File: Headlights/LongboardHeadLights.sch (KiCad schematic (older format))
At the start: 16 parts, among them P1 CONN_01X03, U1 AL8805

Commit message: small schematic changes
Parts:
- C1: footprint (none) -> Capacitors_SMD:C_0805_HandSoldering
- C2: footprint (none) -> Capacitors_SMD:C_0603_HandSoldering
- D4: footprint (none) -> Light_Parts:PowerDI-123
- JP1: footprint (none) -> Connect:GS3
- L1: footprint (none) -> Light_Parts:Inductor_Bourns_6045
- P1: footprint (none) -> Connectors_Molex:Molex_KK-6410-03_03x2.54mm_Straight
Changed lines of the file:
@@
 F 0 "C2" H 3025 3200 50  0000 L CNN
 F 1 "2.2uF" H 3025 3000 50  0000 L CNN
-F 2 "" H 3038 2950 50  0001 C CNN
+F 2 "Capacitors_SMD:C_0603_HandSoldering" H 3038 2950 50  0001 C CNN
 F 3 "" H 3000 3100 50  0000 C CNN
 	1    3000 3100
@@
 F 0 "C1" H 2725 3200 50  0000 L CNN
 F 1 "4.7uF" H 2725 3000 50  0000 L CNN
-F 2 "" H 2738 2950 50  0001 C CNN
+F 2 "Capacitors_SMD:C_0805_HandSoldering" H 2738 2950 50  0001 C CNN
 F 3 "" H 2700 3100 50  0000 C CNN
 	1    2700 3100
@@
 F 0 "L1" V 4400 5100 50  0000 C CNN
 F 1 "INDUCTOR" V 4550 5100 50  0000 C CNN
-F 2 "" H 4450 5100 50  0001 C CNN
+F 2 "Light_Parts:Inductor_Bourns_6045" H 4450 5100 50  0001 C CNN
 F 3 "" H 4450 5100 50  0000 C CNN
 	1    4450 5100
@@
 F 0 "D4" H 5050 3750 50  0000 C CNN
 F 1 "D_Schottky" H 5050 3550 50  0000 C CNN
-F 2 "" H 5050 3650 50  0001 C CNN
+F 2 "Light_Parts:PowerDI-123" H 5050 3650 50  0001 C CNN
 F 3 "" H 5050 3650 50  0000 C CNN
 	1    5050 3650
@@
 F 0 "JP1" H 6300 2850 50  0000 L CNN
 F 1 "JUMPER3" H 6250 3050 50  0000 C BNN
-F 2 "" H 6250 2950 50  0001 C CNN
+F 2 "Connect:GS3" H 6250 2950 50  0001 C CNN
 F 3 "" H 6250 2950 50  0000 C CNN
 	1    6250 2950
@@
 F 0 "P1" H 7800 2800 50  0000 C CNN
 F 1 "CONN_01X03" V 7900 2600 50  0000 C CNN
-F 2 "" H 7800 2600 50  0001 C CNN
+F 2 "Connectors_Molex:Molex_KK-6410-03_03x2.54mm_Straight" H 7800 2600 50  0001 C CNN
 F 3 "" H 7800 2600 50  0000 C CNN
 	1    7800 2600

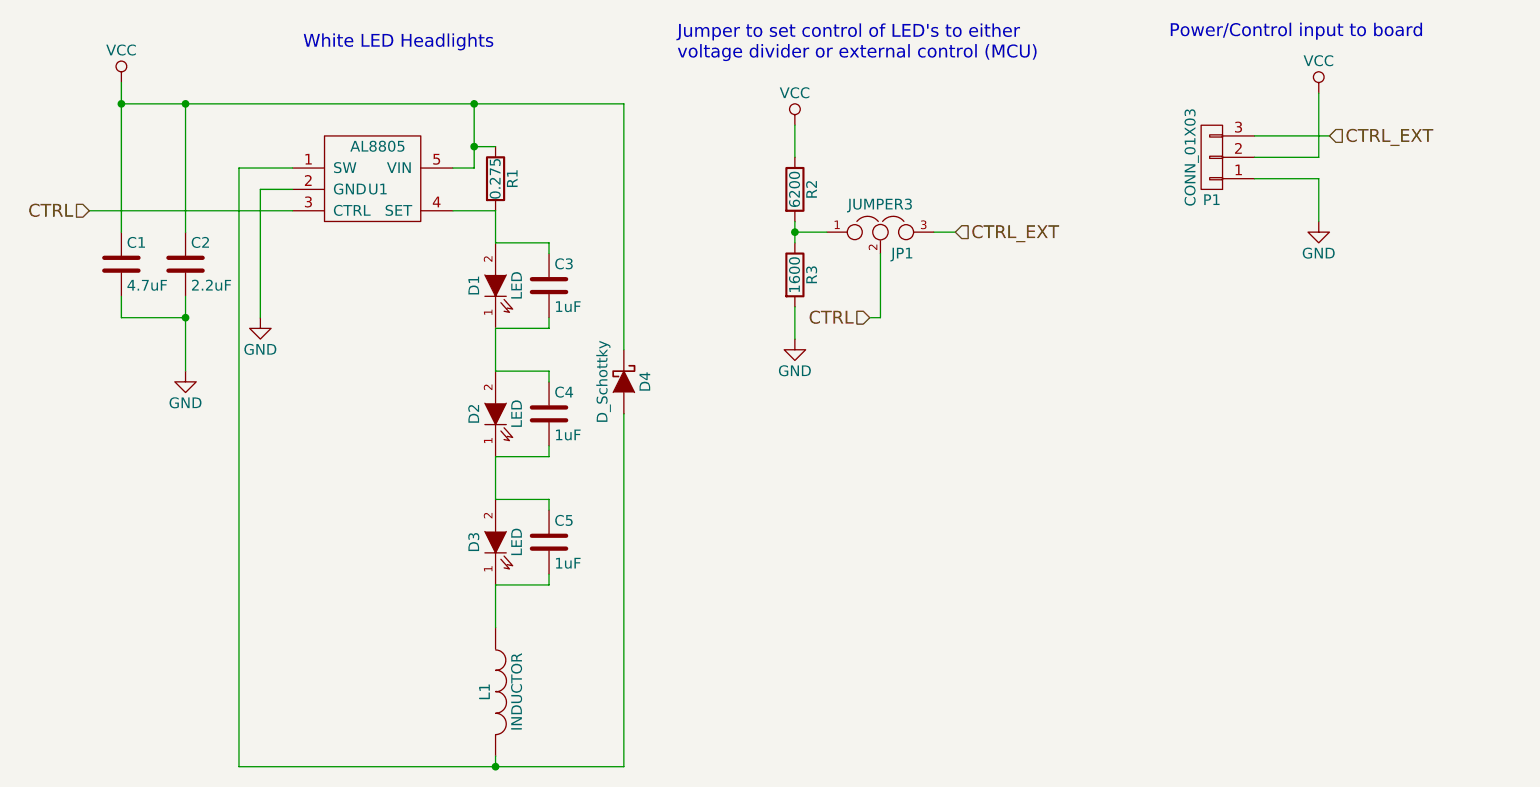
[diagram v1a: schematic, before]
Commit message: finished PCB, updating plan
ditched tail light turn signal idea, now only need one PCB and just
switch out LEDs
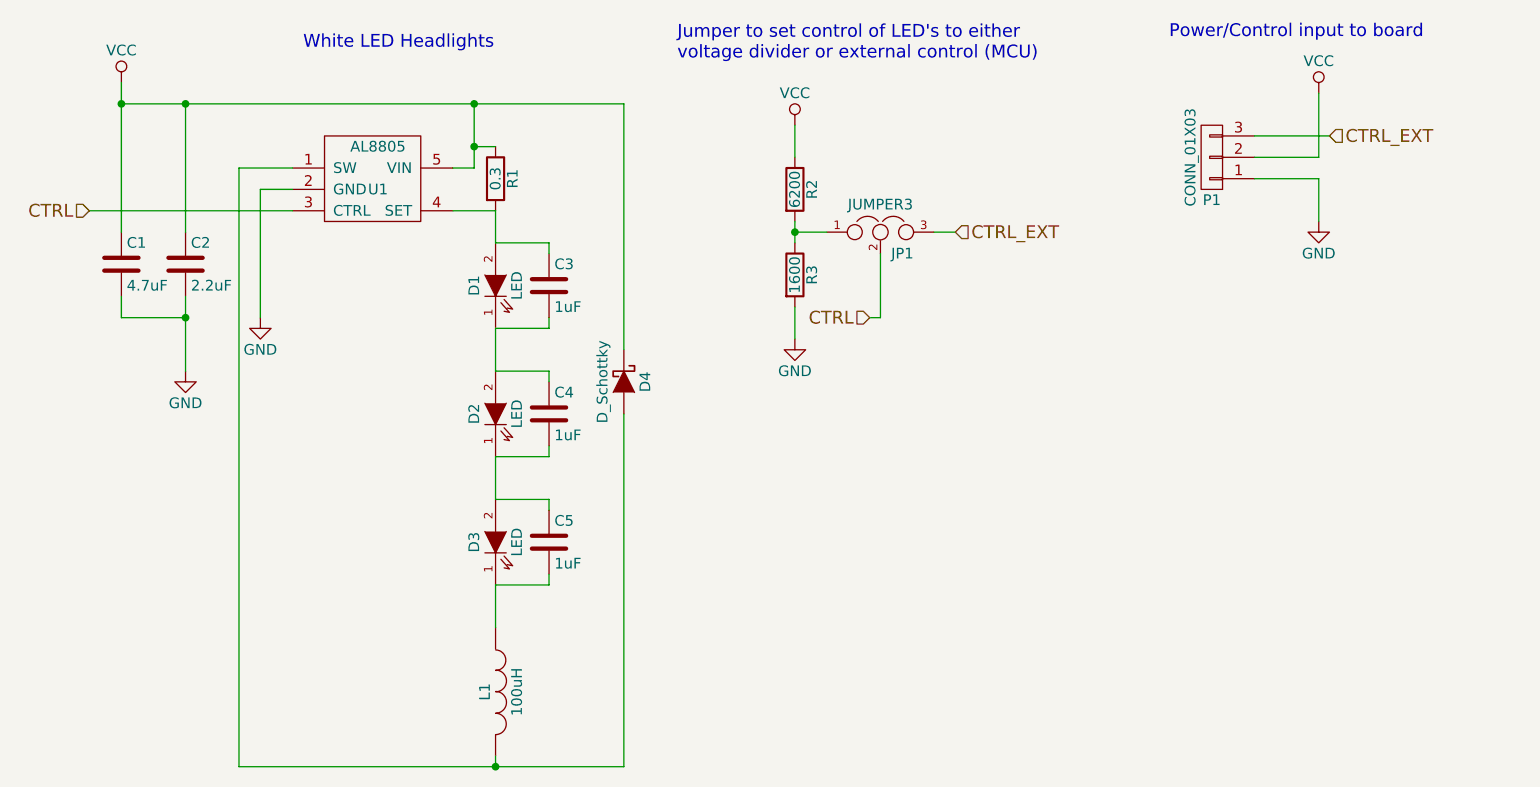
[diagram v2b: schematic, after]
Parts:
- C1: footprint Capacitors_SMD:C_0805_HandSoldering -> Capacitors_SMD:C_0805
- C2, C3, C4, C5: footprint Capacitors_SMD:C_0603_HandSoldering -> Capacitors_SMD:C_0603
- L1: value INDUCTOR -> 100uH
- R1: value 0.275 -> 0.3; footprint Resistors_SMD:R_0603_HandSoldering -> Resistors_SMD:R_0603
- R2, R3: footprint Resistors_SMD:R_0603_HandSoldering -> Resistors_SMD:R_0603
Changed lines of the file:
@@
 P 4450 2700
 F 0 "R1" V 4530 2700 50  0000 C CNN
-F 1 "0.275" V 4450 2700 50  0000 C CNN
-F 2 "Resistors_SMD:R_0603_HandSoldering" V 4380 2700 50  0001 C CNN
+F 1 "0.3" V 4450 2700 50  0000 C CNN
+F 2 "Resistors_SMD:R_0603" V 4380 2700 50  0001 C CNN
 F 3 "" H 4450 2700 50  0000 C CNN
 	1    4450 2700
@@
 F 0 "C5" H 4725 4500 50  0000 L CNN
 F 1 "1uF" H 4725 4300 50  0000 L CNN
-F 2 "Capacitors_SMD:C_0603_HandSoldering" H 4738 4250 50  0001 C CNN
+F 2 "Capacitors_SMD:C_0603" H 4738 4250 50  0001 C CNN
 F 3 "" H 4700 4400 50  0000 C CNN
 	1    4700 4400
@@
 F 0 "C4" H 4725 3900 50  0000 L CNN
 F 1 "1uF" H 4725 3700 50  0000 L CNN
-F 2 "Capacitors_SMD:C_0603_HandSoldering" H 4738 3650 50  0001 C CNN
+F 2 "Capacitors_SMD:C_0603" H 4738 3650 50  0001 C CNN
 F 3 "" H 4700 3800 50  0000 C CNN
 	1    4700 3800
@@
 F 0 "C3" H 4725 3300 50  0000 L CNN
 F 1 "1uF" H 4725 3100 50  0000 L CNN
-F 2 "Capacitors_SMD:C_0603_HandSoldering" H 4738 3050 50  0001 C CNN
+F 2 "Capacitors_SMD:C_0603" H 4738 3050 50  0001 C CNN
 F 3 "" H 4700 3200 50  0000 C CNN
 	1    4700 3200
@@
 F 0 "C2" H 3025 3200 50  0000 L CNN
 F 1 "2.2uF" H 3025 3000 50  0000 L CNN
-F 2 "Capacitors_SMD:C_0603_HandSoldering" H 3038 2950 50  0001 C CNN
+F 2 "Capacitors_SMD:C_0603" H 3038 2950 50  0001 C CNN
 F 3 "" H 3000 3100 50  0000 C CNN
 	1    3000 3100
@@
 F 0 "C1" H 2725 3200 50  0000 L CNN
 F 1 "4.7uF" H 2725 3000 50  0000 L CNN
-F 2 "Capacitors_SMD:C_0805_HandSoldering" H 2738 2950 50  0001 C CNN
+F 2 "Capacitors_SMD:C_0805" H 2738 2950 50  0001 C CNN
 F 3 "" H 2700 3100 50  0000 C CNN
 	1    2700 3100
@@
 P 4450 5100
 F 0 "L1" V 4400 5100 50  0000 C CNN
-F 1 "INDUCTOR" V 4550 5100 50  0000 C CNN
+F 1 "100uH" V 4550 5100 50  0000 C CNN
 F 2 "Light_Parts:Inductor_Bourns_6045" H 4450 5100 50  0001 C CNN
 F 3 "" H 4450 5100 50  0000 C CNN
@@
 F 0 "R2" V 5930 2750 50  0000 C CNN
 F 1 "6200" V 5850 2750 50  0000 C CNN
-F 2 "Resistors_SMD:R_0603_HandSoldering" V 5780 2750 50  0001 C CNN
+F 2 "Resistors_SMD:R_0603" V 5780 2750 50  0001 C CNN
 F 3 "" H 5850 2750 50  0000 C CNN
 	1    5850 2750
@@
 F 0 "R3" V 5930 3150 50  0000 C CNN
 F 1 "1600" V 5850 3150 50  0000 C CNN
-F 2 "Resistors_SMD:R_0603_HandSoldering" V 5780 3150 50  0001 C CNN
+F 2 "Resistors_SMD:R_0603" V 5780 3150 50  0001 C CNN
 F 3 "" H 5850 3150 50  0000 C CNN
 	1    5850 3150

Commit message: couple quick changes
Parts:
- R2: value 6200 -> 38K
- R3: value 1600 -> 10K
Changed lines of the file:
@@
 P 5850 2750
 F 0 "R2" V 5930 2750 50  0000 C CNN
-F 1 "6200" V 5850 2750 50  0000 C CNN
+F 1 "38K" V 5850 2750 50  0000 C CNN
 F 2 "Resistors_SMD:R_0603" V 5780 2750 50  0001 C CNN
 F 3 "" H 5850 2750 50  0000 C CNN
@@
 P 5850 3150
 F 0 "R3" V 5930 3150 50  0000 C CNN
-F 1 "1600" V 5850 3150 50  0000 C CNN
+F 1 "10K" V 5850 3150 50  0000 C CNN
 F 2 "Resistors_SMD:R_0603" V 5780 3150 50  0001 C CNN
 F 3 "" H 5850 3150 50  0000 C CNN

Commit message: updating designs for newest revision; removing unneeded files
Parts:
- removed C1: 4.7uF, Capacitors_SMD:C_0805, symbol C
- removed C2: 2.2uF, Capacitors_SMD:C_0603, symbol C
- removed C3, C4, C5: 1uF, Capacitors_SMD:C_0603, symbol C
- removed D3: LED, LEDs:LED-XP-G_CREE, symbol LED
- removed D4: D_Schottky, Light_Parts:PowerDI-123, symbol D_Schottky
- removed JP1: JUMPER3, Connect:GS3, symbol JUMPER3
- removed L1: 100uH, Light_Parts:Inductor_Bourns_6045, symbol INDUCTOR
- removed R1: 0.3, Resistors_SMD:R_0603, symbol R
- removed R2: 38K, Resistors_SMD:R_0603, symbol R
- removed R3: 10K, Resistors_SMD:R_0603, symbol R
- removed U1: AL8805, TO_SOT_Packages_SMD:SOT-23-5, symbol AL8805
- D1, D2: symbol LED -> LED-RESCUE-LongboardHeadLights
- P1: footprint Connectors_Molex:Molex_KK-6410-03_03x2.54mm_Straight -> Connectors_JST:JST_EH_B02B-EH-A_02x2.50mm_Straight; symbol CONN_01X03 -> Conn_01x02
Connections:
- net GND is gone; now on an unnamed net: P1.1 (Pin_1)
- net VCC is gone; now on an unnamed net: P1.2 (Pin_2)
- removed net CTRL_EXT: P1.3 (P3)
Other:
- note added: "Power In"
- note added: "Power Out"
- note removed: "Jumper to set control of LED's to either\nvoltage divider or external control (MCU)"
- note removed: "Power/Control input to board"
- note removed: "White LED Headlights"
- moved on the sheet: D1, D2
